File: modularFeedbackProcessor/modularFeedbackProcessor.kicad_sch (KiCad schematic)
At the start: 81 parts, among them J1 Input, J2 Feedback, J3 Inhibit, J4 DryWet, J5 Rate, J6 EffectRouteIn, J7 EffectRouteOut, J8 EffectsDryWet, J9 Output, Q1 Q_PMOS_GDS, Q2 NJFET, SW1 EffectsRouting, U1 TL074, U2 TL074, U3 TL074, U4 TL074, U5 LM13700, U6 V3205, U7 CD4046, U8 LF398_DIP8

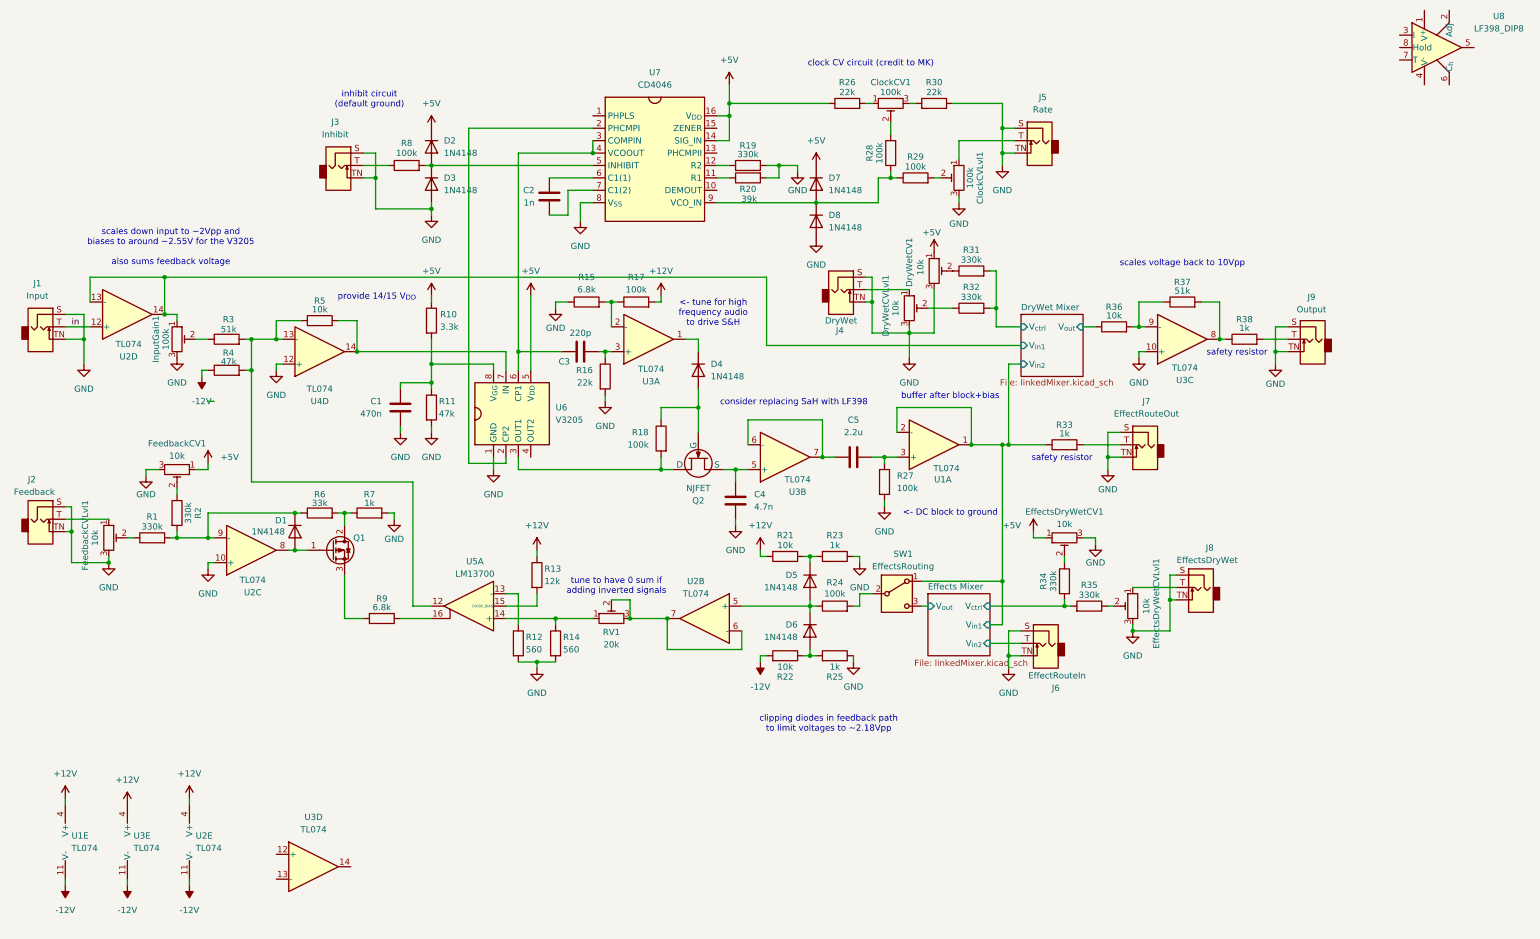
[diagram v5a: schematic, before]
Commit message: added all footprints, beginning to work on ERC errors
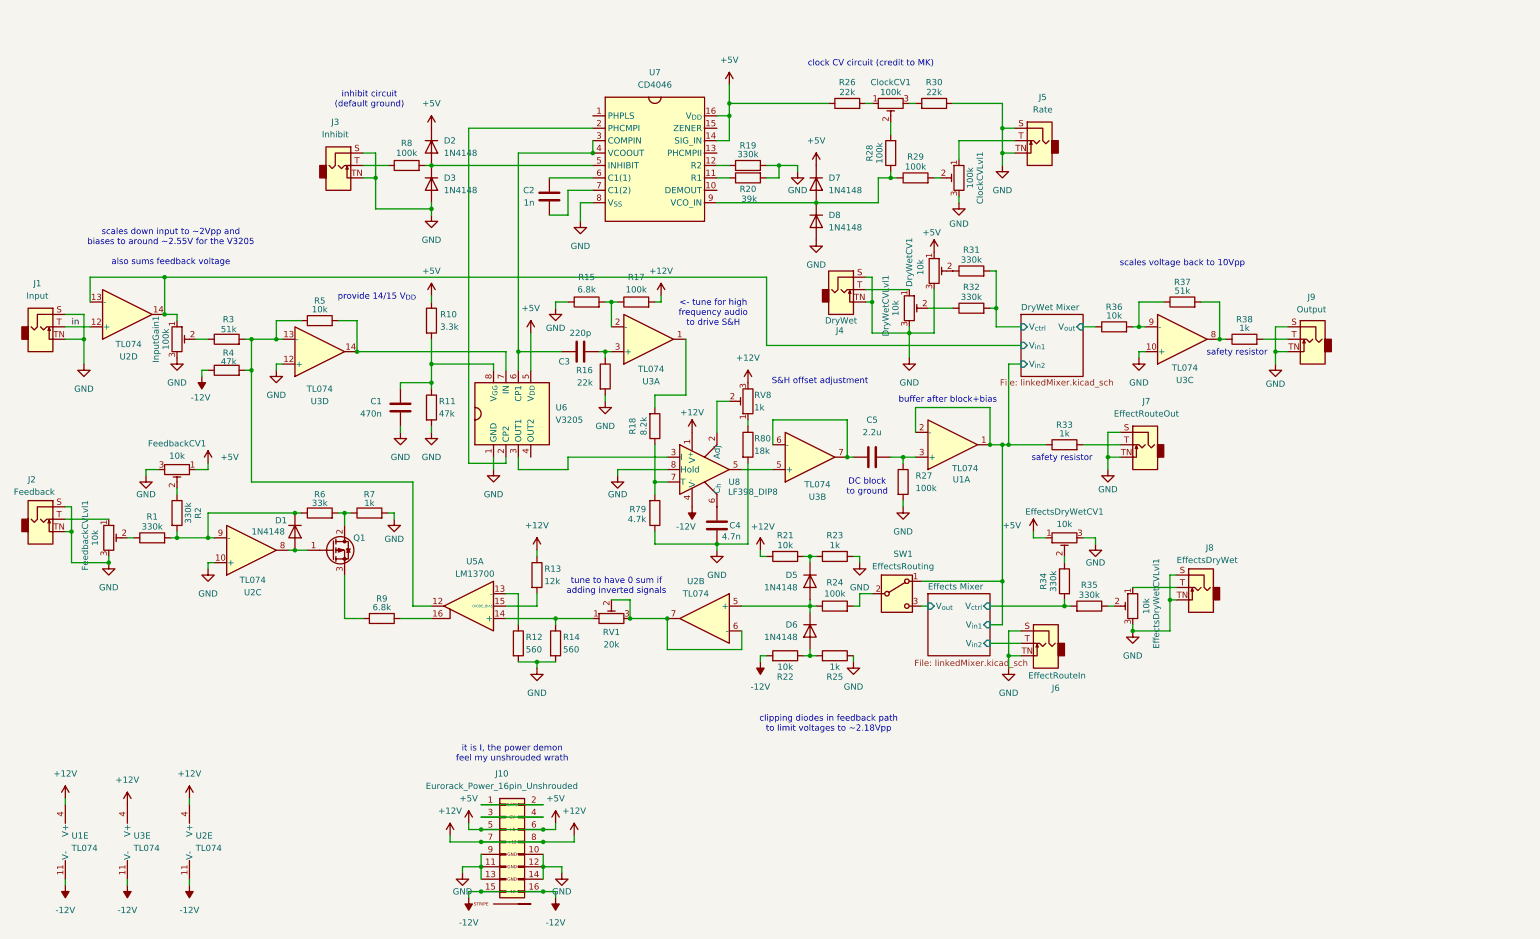
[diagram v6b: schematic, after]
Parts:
- removed D4: 1N4148, Diode_THT:D_DO-35_SOD27_P7.62mm_Horizontal, symbol Diode:1N4148
- removed Q2: NJFET, symbol Simulation_SPICE:NJFET
- removed U4: TL074, symbol Amplifier_Operational:TL074
- added J10: Eurorack_Power_16pin_Unshrouded, 4ms_Connector:Pins_2x08_2.54mm_TH_EuroPower, symbol PCM_4ms_Connector:Eurorack_Power_16pin_Unshrouded
- added R79: 4.7k, Resistor_SMD:R_0805_2012Metric_Pad1.20x1.40mm_HandSolder, symbol Device:R
- added R80: 18k, Resistor_SMD:R_0805_2012Metric_Pad1.20x1.40mm_HandSolder, symbol Device:R
- added RV8: 1k, Potentiometer_THT:Potentiometer_Vishay_T73XW_Horizontal, symbol Device:R_Potentiometer_Trim
- C1, C2, C3, C4: footprint Capacitor_THT:C_Disc_D4.7mm_W2.5mm_P5.00mm -> Capacitor_SMD:C_0805_2012Metric_Pad1.18x1.45mm_HandSolder
- C5: footprint Capacitor_THT:CP_Radial_D5.0mm_P2.50mm -> Capacitor_SMD:C_0805_2012Metric_Pad1.18x1.45mm_HandSolder
- ClockCV1, ClockCVLvl1, DryWetCV1, DryWetCVLvl1, EffectsDryWetCV1, EffectsDryWetCVLvl1, FeedbackCV1, FeedbackCVLvl1, InputGain1: footprint (none) -> PCM_Eurocad:Alpha9mmPot
- Q1: footprint (none) -> Package_TO_SOT_THT:TO-220-3_Vertical
- R1, R10, R11, R12, R13, R14, R15, R16, R17, R19, R2, R20, R21, R22, R23, R24, R25, R26, R27, R28, R29, R3, R30, R31, R32, R33, R34, R35, R36, R37, R38, R4, R5, R6, R7, R8, R9: footprint (none) -> Resistor_SMD:R_0805_2012Metric_Pad1.20x1.40mm_HandSolder
- R18: value 100k -> 8.2k; footprint (none) -> Resistor_SMD:R_0805_2012Metric_Pad1.20x1.40mm_HandSolder
- RV1: footprint (none) -> Potentiometer_THT:Potentiometer_Vishay_T73XW_Horizontal
- SW1: footprint (none) -> PCM_4ms_Switch:Switch_Toggle_SPDT_SubMini
- U1, U2, U3, U5: footprint (none) -> Package_DIP:DIP-14_W7.62mm_LongPads
- U6: footprint (none) -> Package_DIP:DIP-14_W7.62mm_LongPads_8pin
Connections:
- net +12V: now also U8.1 (V^{+}), J10.7 (12V), J10.8 (+12V), RV8.3
- net +5V: now also J10.5 (+12V), J10.6 (P6)
- net -12V: now also U8.4 (V^{-}), J10.15 (-12V), J10.16 (P16)
- net GND: now also U3.12 (+), U8.8 (Hold), J10.10 (GND), J10.11 (GND), J10.12 (GND), J10.13 (-12), J10.14 (-12V), J10.9 (GND), R79.1, R80.2
- net at R3.2, R4.2, R5.1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: now also U3.13 (-)
- net at U6.3 (OUT1): now also U8.3 (I); no longer R18.2
- net at R18.1: now also U8.7 (T), R79.2
- net at C4.1: now also U8.6 (C_{h}); no longer U3.5 (+)
- net at R5.2, U6.7 (IN): now also U3.14
- net at U3.1: now also R18.2
- net at U8.2 (Adj): now also RV8.2
- net at U8.5: now also U3.5 (+)
- new net: J10.1 (P1), J10.2 (P2)
- new net: J10.3 (P3), J10.4 (P4)
- new net: R80.1, RV8.1
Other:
- note added: "DC block to ground"
- note added: "S&H offset adjustment"
- note added: "it is I, the power demon feel my unshrouded wrath"
- note removed: "<- DC block to ground"
- note removed: "consider replacing SaH with LF398"
- moved on the sheet: C4, C5, R27, U1A, U3B, U3D, U8

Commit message: lots of friggin progress. finished footprint work, and have just finished grouping. Now I will start to connect each group internally.
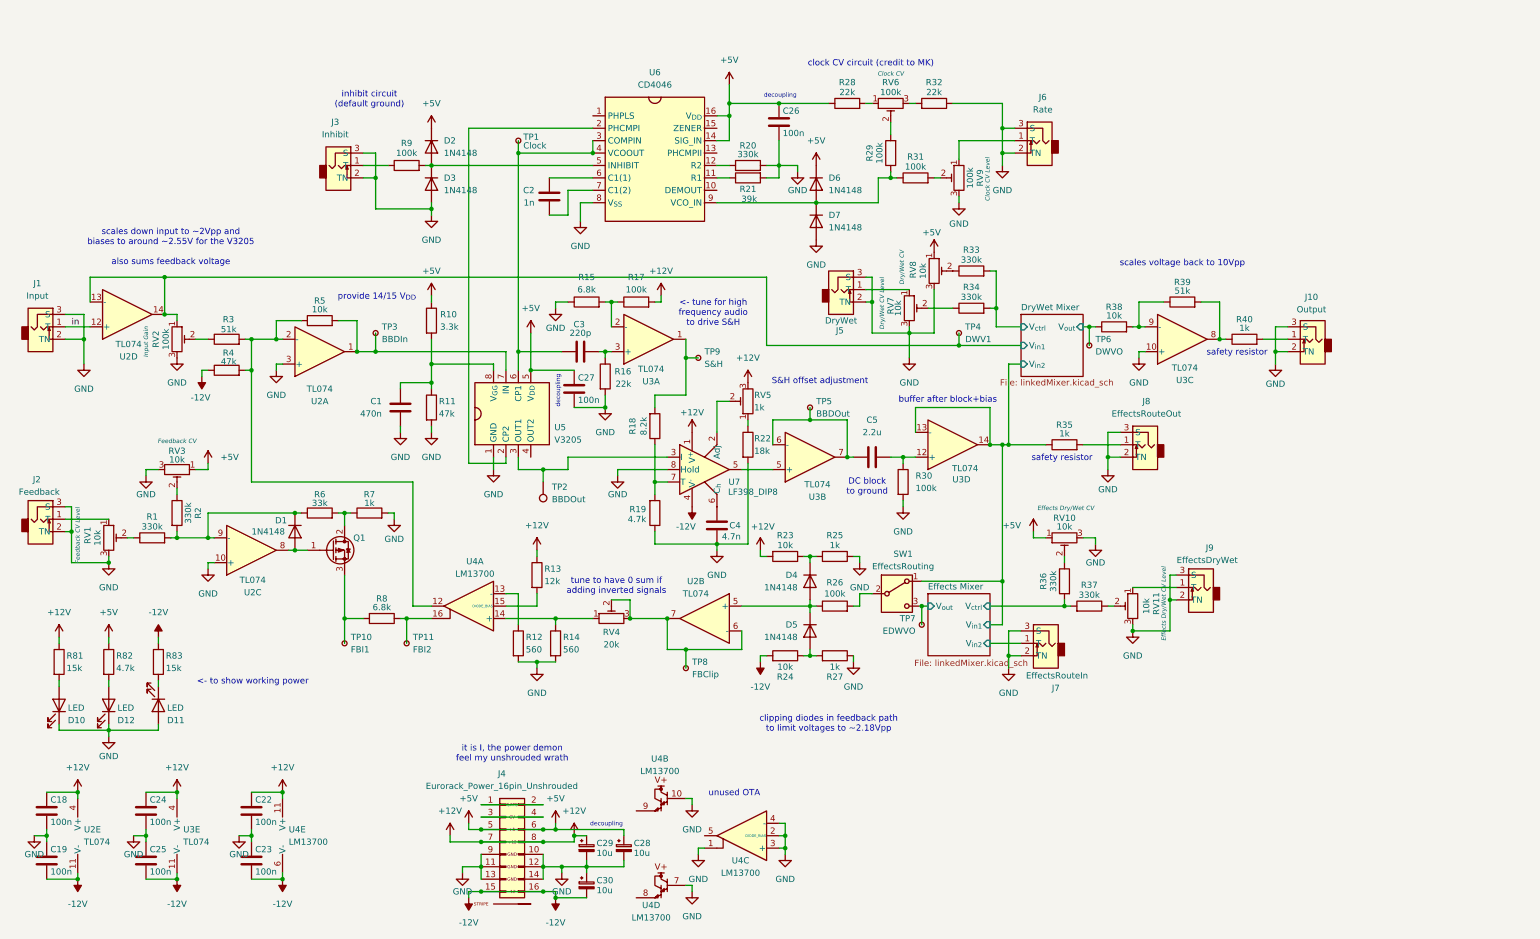
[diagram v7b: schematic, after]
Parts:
- removed unit 5 of U1
- added C18, C19, C22, C23, C24, C25, C26, C27: 100n, Capacitor_SMD:C_0805_2012Metric_Pad1.18x1.45mm_HandSolder, symbol Device:C
- added C28, C29, C30: 10u, Capacitor_THT:CP_Radial_D5.0mm_P2.00mm, symbol Device:C_Polarized_Small
- added D10, D11, D12: LED, LED_THT:LED_D5.0mm, symbol Device:LED
- added R81, R83: 15k, Resistor_SMD:R_0805_2012Metric_Pad1.20x1.40mm_HandSolder, symbol Device:R
- added R82: 4.7k, Resistor_SMD:R_0805_2012Metric_Pad1.20x1.40mm_HandSolder, symbol Device:R
- added TP1: Clock, PCM_4ms_TestPoint:TestPoint_Pad_06, symbol PCM_4ms_Connector:TestPoint_Small
- added TP10: FBI1, PCM_4ms_TestPoint:TestPoint_Pad_06, symbol PCM_4ms_Connector:TestPoint_Small
- added TP11: FBI2, PCM_4ms_TestPoint:TestPoint_Pad_06, symbol PCM_4ms_Connector:TestPoint_Small
- added TP2: BBDOut, PCM_4ms_TestPoint:TestPoint_Pad_06, symbol PCM_4ms_Connector:TestPoint
- added TP3: BBDIn, PCM_4ms_TestPoint:TestPoint_Pad_06, symbol PCM_4ms_Connector:TestPoint_Small
- added TP4: DWV1, PCM_4ms_TestPoint:TestPoint_Pad_06, symbol PCM_4ms_Connector:TestPoint_Small
- added TP5: BBDOut, PCM_4ms_TestPoint:TestPoint_Pad_06, symbol PCM_4ms_Connector:TestPoint_Small
- added TP6: DWVO, PCM_4ms_TestPoint:TestPoint_Pad_06, symbol PCM_4ms_Connector:TestPoint_Small
- added TP7: EDWVO, PCM_4ms_TestPoint:TestPoint_Pad_06, symbol PCM_4ms_Connector:TestPoint_Small
- added TP8: FBClip, PCM_4ms_TestPoint:TestPoint_Pad_06, symbol PCM_4ms_Connector:TestPoint_Small
- added TP9: S&H, PCM_4ms_TestPoint:TestPoint_Pad_06, symbol PCM_4ms_Connector:TestPoint_Small
- J4: renamed from J10; footprint 4ms_Connector:Pins_2x08_2.54mm_TH_EuroPower -> PCM_4ms_Connector:Pins_2x08_2.54mm_TH_EuroPower
- J7: renamed from J6; value EffectRouteIn -> EffectsRouteIn
- J8: renamed from J7; value EffectRouteOut -> EffectsRouteOut
- RV1: renamed from FeedbackCVLvl1; Parameter (none) -> Feedback CV Level
- RV10: renamed from EffectsDryWetCV1; Parameter (none) -> Effects Dry/Wet CV
- RV11: renamed from EffectsDryWetCVLvl1; Parameter (none) -> Effects Dry/Wet CV Level
- RV2: renamed from InputGain1; Parameter (none) -> Input Gain
- RV3: renamed from FeedbackCV1; Parameter (none) -> Feedback CV
- RV6: renamed from ClockCV1; Parameter (none) -> Clock CV
- RV7: renamed from DryWetCVLvl1; Parameter (none) -> Dry/Wet CV Level
- RV8: renamed from DryWetCV1; Parameter (none) -> Dry/Wet CV
- RV9: renamed from ClockCVLvl1; Parameter (none) -> Clock CV Level
- U4: renamed from U5; footprint Package_DIP:DIP-14_W7.62mm_LongPads -> Package_DIP:DIP-16_W7.62mm_LongPads
- U6: renamed from U7; footprint (none) -> Package_DIP:DIP-16_W7.62mm_LongPads; now in the parts list
- renumbered D5 to D4, D6 to D5, D7 to D6, D8 to D7, J9 to J10, J4 to J5, J5 to J6, J8 to J9, R79 to R19, R19 to R20, R20 to R21, R80 to R22, R21 to R23, R22 to R24, R23 to R25, R24 to R26, R25 to R27, R26 to R28, R28 to R29, R27 to R30, R29 to R31, R30 to R32, R31 to R33, R32 to R34, R33 to R35, R34 to R36, R35 to R37, R36 to R38, R37 to R39, R38 to R40, R9 to R8, R8 to R9, RV1 to RV4, RV8 to RV5, U3 to U2, U1 to U3, U6 to U5, U8 to U7
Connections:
- net +12V: now also U4.11 (V+), C18.1, C22.1, C24.1, C29.1, R81.1
- net +5V: now also C26.1, C27.1, C28.1, R82.1
- net -12V: now also U4.6 (V-), C19.2, C23.2, C25.2, C30.2, R83.1
- net DryWet Mixer/V_{in1}: now also TP4.1
- net DryWet Mixer/V_{in2}: now also U3.13 (-), U3.14; no longer U3.1, U3.2 (-)
- net DryWet Mixer/V_{out}: now also TP6.1
- net Effects Mixer/V_{in2}: now also J7.1 (T); no longer J7.T
- net Effects Mixer/V_{out}: now also TP7.1
- net GND: now also J1.2 (TN), J1.3 (S), J10.2 (TN), J10.3 (S), J2.2 (TN), J2.3 (S), J3.2 (TN), J3.3 (S), J5.2 (TN), J5.3 (S), J6.2 (TN), J6.3 (S), J7.2 (TN), J7.3 (S), J8.2 (TN), J8.3 (S), J9.2 (TN), J9.3 (S), U2.3 (+), U4.1, U4.10, U4.2 (DIODE_BIAS), U4.3 (+), U4.4 (-), U4.7, C18.2, C19.1, C22.2, C23.1, C24.2, C25.1, C26.2, C27.2, C28.2, C29.2, C30.1, D10.1 (K), D11.2 (A), D12.1 (K); no longer J1.S, J1.TN, J10.S, J10.TN, J2.S, J2.TN, J3.S, J3.TN, J5.S, J5.TN, J6.S, J6.TN, J7.S, J7.TN, J8.S, J8.TN, J9.S, J9.TN, U2.12 (+)
- net in: now also J1.1 (T); no longer J1.T
- net at R3.2, R4.2, R5.1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: now also U2.2 (-); no longer U2.13 (-)
- net at R8.1, U4.16: now also TP11.1
- net at C5.1, R30.1: now also U3.12 (+); no longer U3.3 (+)
- net at C5.2, U3.6 (-), U3.7: now also TP5.1
- net at RV9.1: now also J6.1 (T); no longer J6.T
- net at Q1.3 (S), R8.2: now also TP10.1
- net at R35.2: now also J8.1 (T); no longer J8.T
- net at R40.2: now also J10.1 (T); no longer J10.T
- net at RV11.1: now also J9.1 (T); no longer J9.T
- net at R5.2, U5.7 (IN): now also U2.1, TP3.1; no longer U2.14
- net at RV1.1: now also J2.1 (T); no longer J2.T
- net at U5.3 (OUT1), U7.3 (I): now also TP2.1
- net at C3.1, U5.6 (CP1), U6.3 (COMPIN)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: now also TP1.1
- net at R18.2, U3.1: now also TP9.1
- net at R9.1: now also J3.1 (T); no longer J3.T
- net at RV7.1: now also J5.1 (T); no longer J5.T
- net at RV4.2, RV4.3, U2.6 (-)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: now also TP8.1
- new net: D12.2 (A), R82.2
- new net: D10.2 (A), R81.2
- new net: D11.1 (K), R83.2
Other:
- note added: "<- to show working power"
- note added: "decoupling"
- note added: "unused OTA"
- moved on the sheet: U2E, U3E

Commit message: save before i mess something up
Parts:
- added unit 1 of U3
- added unit 3 of U3
- added unit 5 of U3
- added unit 4 of U3
- TP8: renamed from TP5; value BBDOut -> S&HOut
- renumbered C18 to C1, C3 to C10, C29 to C11, C30 to C12, C28 to C13, C4 to C14, C26 to C15, C5 to C16, C19 to C2, C24 to C3, C25 to C4, C22 to C5, C23 to C6, C1 to C7, C2 to C8, C27 to C9, D10 to D1, D7 to D10, D12 to D2, D11 to D3, D1 to D4, D2 to D5, D3 to D6, D4 to D7, D5 to D8, D6 to D9, R81 to R1, R7 to R10, R8 to R11, R9 to R12, R10 to R13, R11 to R14, R12 to R15, R13 to R16, R14 to R17, R15 to R18, R16 to R19, R82 to R2, R17 to R20, R18 to R21, R19 to R22, R20 to R23, R21 to R24, R22 to R25, R23 to R26, R24 to R27, R25 to R28, R26 to R29, R1 to R3, R27 to R30, R28 to R31, R29 to R32, R30 to R33, R31 to R34, R32 to R35, R33 to R36, R34 to R37, R35 to R38, R36 to R39, R83 to R4, R37 to R40, R38 to R41, R39 to R42, R40 to R43, R2 to R5, R3 to R6, R4 to R7, R5 to R8, R6 to R9, TP10 to TP1, TP4 to TP10, TP6 to TP11, TP3 to TP2, TP11 to TP3, TP1 to TP4, TP2 to TP5, TP8 to TP6, TP9 to TP7, TP7 to TP9, U2 to U1, U3 to U2, U4 to U3, U5 to U4, U6 to U5, U7 to U6
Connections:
- net +12V: now also U3.11 (V+); no longer U3.11 (V+)
- net -12V: now also U3.6 (V-); no longer U3.6 (V-)
- net GND: now also U3.1, U3.2 (DIODE_BIAS), U3.3 (+), U3.4 (-), U3.7; no longer U3.1, U3.2 (DIODE_BIAS), U3.3 (+), U3.4 (-), U3.7
- net at R6.2, R7.2, R8.1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: now also U3.12; no longer U3.12
- net at R15.1: now also U3.13 (-); no longer U3.13 (-)
- net at R17.1, RV4.1: now also U3.14 (+); no longer U3.14 (+)
- net at R16.2: now also U3.15 (DIODE_BIAS); no longer U3.15 (DIODE_BIAS)
- net at R11.1, TP3.1: now also U3.16; no longer U3.16
- net Effects Mixer/V_{ctrl} renamed Effects DryWet Mixer/V_{ctrl}
- net Effects Mixer/V_{in2} renamed Effects DryWet Mixer/V_{in2}
- net Effects Mixer/V_{out} renamed Effects DryWet Mixer/V_{out}
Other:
- removed sheet Effects Mixer
- added sheet Effects DryWet Mixer (Mixer.kicad_sch)
- sheet DryWet Mixer: file linkedMixer.kicad_sch -> Mixer.kicad_sch
